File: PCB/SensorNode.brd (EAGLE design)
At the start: 93.6 x 69.8 mm, 68 parts, among them J4 USB_MINI-B_SMT, Q1 CMA-4544PF-W, Q2 600mA/40V, Q3 600mA/40V, U1 MAX4466EXK+T, U2 ESP-WROOM-32, U3 Si7021-A20, U4 MCP73831, U5 TSL2561, U6 CP2104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

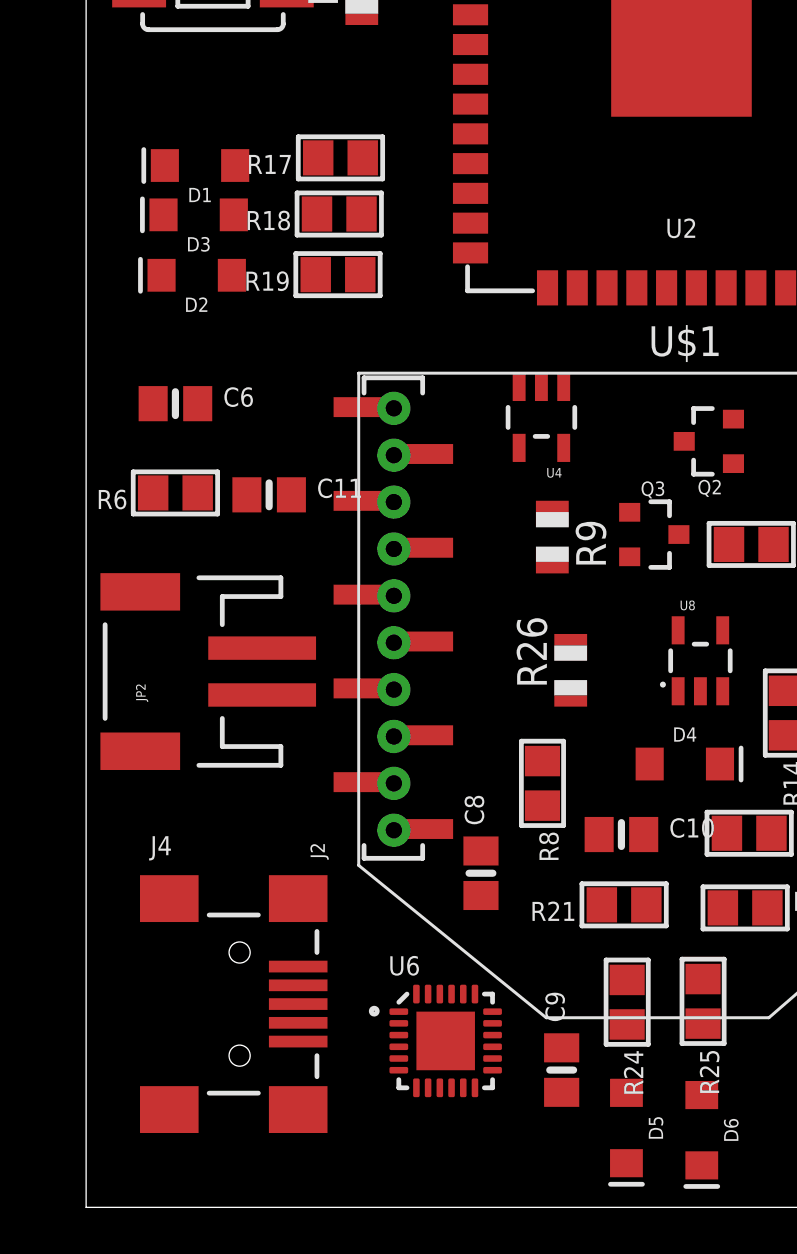
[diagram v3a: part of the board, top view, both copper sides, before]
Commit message: Created Android Wear App
Sets the smart watch's bluetooth to discoverable.
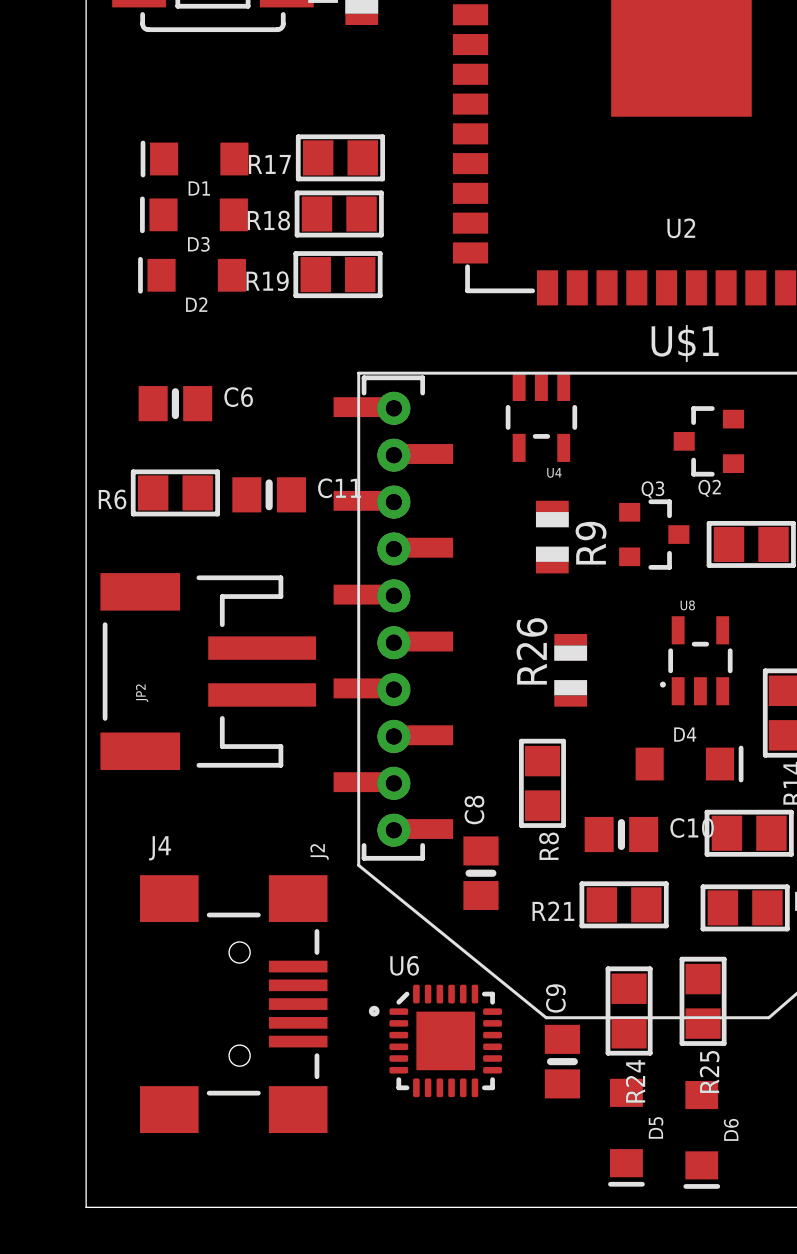
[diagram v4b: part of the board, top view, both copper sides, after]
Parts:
- moved R24 0.39 mm to (21.9, 41.4)
- moved C9 0.36 mm to (19.1, 39.2)
- moved D1 0.28 mm to (3.56, 77.7)
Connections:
- net VIN renamed VBUS
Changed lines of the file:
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@@
 <attribute name="PROD_ID" value="BATT-13243" x="-8.066809375" y="98.5227625" size="1.778" layer="27" rot="R180" display="off"/>
 </element>
-<element name="D1" library="SparkFun-LED" package="LED-1206" value="BLUE" x="3.590128125" y="77.468071875" rot="R180">
-<attribute name="PROD_ID" value="DIO-09911" x="3.590128125" y="77.468071875" size="1.778" layer="27" rot="R180" display="off"/>
+<element name="D1" library="SparkFun-LED" package="LED-1206" value="BLUE" x="3.557346875" y="77.746625" rot="R180">
+<attribute name="PROD_ID" value="DIO-09911" x="3.557346875" y="77.746625" size="1.778" layer="27" rot="R180" display="off"/>
 </element>
 <element name="D2" library="SparkFun-LED" package="LED-1206" value="GREEN" x="3.448509375" y="72.785596875" rot="R180">
@@
 <attribute name="PROD_ID" value="DIO-00862" x="24.996034375" y="36.311871875" size="1.778" layer="27" rot="R270" display="off"/>
 </element>
-<element name="R24" library="microbuilder" package="0805" value="???" x="21.813565625" y="41.774221875" rot="R270"/>
+<element name="R24" library="microbuilder" package="0805" value="???" x="21.89551875" y="41.397359375" rot="R270"/>
 <element name="R25" library="microbuilder" package="0805" value="???" x="25.051178125" y="41.810359375" rot="R270"/>
-<element name="C9" library="microbuilder" package="0805-NO" value="4.7uF" x="19.0186" y="38.877525" rot="R90"/>
+<element name="C9" library="microbuilder" package="0805-NO" value="4.7uF" x="19.05138125" y="39.238003125" rot="R90"/>
 <element name="R8" library="microbuilder" package="0805" value="4.7K" x="18.199771875" y="51.10983125" rot="R270"/>
 <element name="C11" library="microbuilder" package="0805-NO" value="0.1uF" x="6.538284375" y="63.41988125"/>
@@
 <wire x1="12.070421875" y1="40.870465625" x2="15.575896875" y2="46.32528125" width="0" layer="19" extent="1-1"/>
 <wire x1="7.778903125" y1="40.093175" x2="12.070421875" y2="40.870465625" width="0" layer="19" extent="1-1"/>
-<wire x1="19.0186" y1="37.927525" x2="12.070421875" y2="40.870465625" width="0" layer="19" extent="1-1"/>
-<wire x1="21.78253125" y1="34.9056" x2="19.0186" y2="37.927525" width="0" layer="19" extent="1-1"/>
+<wire x1="19.05138125" y1="38.288003125" x2="12.070421875" y2="40.870465625" width="0" layer="19" extent="1-1"/>
+<wire x1="21.78253125" y1="34.9056" x2="19.05138125" y2="38.288003125" width="0" layer="19" extent="1-1"/>
 <wire x1="24.996034375" y1="34.811871875" x2="21.78253125" y2="34.9056" width="0" layer="19" extent="1-1"/>
 <wire x1="32.40484375" y1="34.432371875" x2="24.996034375" y2="34.811871875" width="0" layer="19" extent="1-1"/>
@@
 <wire x1="1.948509375" y1="72.785596875" x2="1.59" y2="67.31" width="0" layer="19" extent="1-1"/>
 <wire x1="2.03210625" y1="75.364025" x2="1.948509375" y2="72.785596875" width="0" layer="19" extent="1-1"/>
-<wire x1="2.090128125" y1="77.468071875" x2="2.03210625" y2="75.364025" width="0" layer="19" extent="1-1"/>
+<wire x1="2.057346875" y1="77.746625" x2="2.03210625" y2="75.364025" width="0" layer="19" extent="1-1"/>
 <wire x1="6.24" y1="54.88" x2="7.488284375" y2="63.41988125" width="0" layer="19" extent="1-1"/>
 <wire x1="15.13" y1="90.25" x2="26.67" y2="100.33" width="0" layer="19" extent="1-1"/>
@@
 <contactref element="U2" pad="27"/>
 </signal>
-<signal name="VIN">
+<signal name="VBUS">
 <contactref element="U4" pad="4"/>
 <contactref element="R21" pad="1"/>
@@
 <contactref element="R17" pad="2"/>
 <contactref element="D1" pad="A"/>
-<wire x1="5.090128125" y1="77.468071875" x2="8.631190625" y2="77.7948125" width="0" layer="19" extent="1-1"/>
+<wire x1="5.057346875" y1="77.746625" x2="8.631190625" y2="77.7948125" width="0" layer="19" extent="1-1"/>
 </signal>
 <signal name="N$27">
@@
 <contactref element="D5" pad="A"/>
 <contactref element="R24" pad="2"/>
-<wire x1="21.78253125" y1="37.9056" x2="21.813565625" y2="40.824221875" width="0" layer="19" extent="1-1"/>
+<wire x1="21.78253125" y1="37.9056" x2="21.89551875" y2="40.447359375" width="0" layer="19" extent="1-1"/>
 </signal>
 <signal name="N$42">
 <contactref element="U6" pad="14"/>
 <contactref element="R24" pad="1"/>
-<wire x1="16.070421875" y1="39.370465625" x2="21.813565625" y2="42.724221875" width="0" layer="19" extent="1-1"/>
+<wire x1="16.070421875" y1="39.370465625" x2="21.89551875" y2="42.347359375" width="0" layer="19" extent="1-1"/>
 </signal>
 <signal name="N$43">
@@
 <contactref element="U6" pad="16"/>
 <contactref element="C9" pad="2"/>
-<wire x1="16.070421875" y1="40.370465625" x2="19.0186" y2="39.827525" width="0" layer="19" extent="1-1"/>
+<wire x1="16.070421875" y1="40.370465625" x2="19.05138125" y2="40.188003125" width="0" layer="19" extent="1-1"/>
 </signal>
 <signal name="N$11">

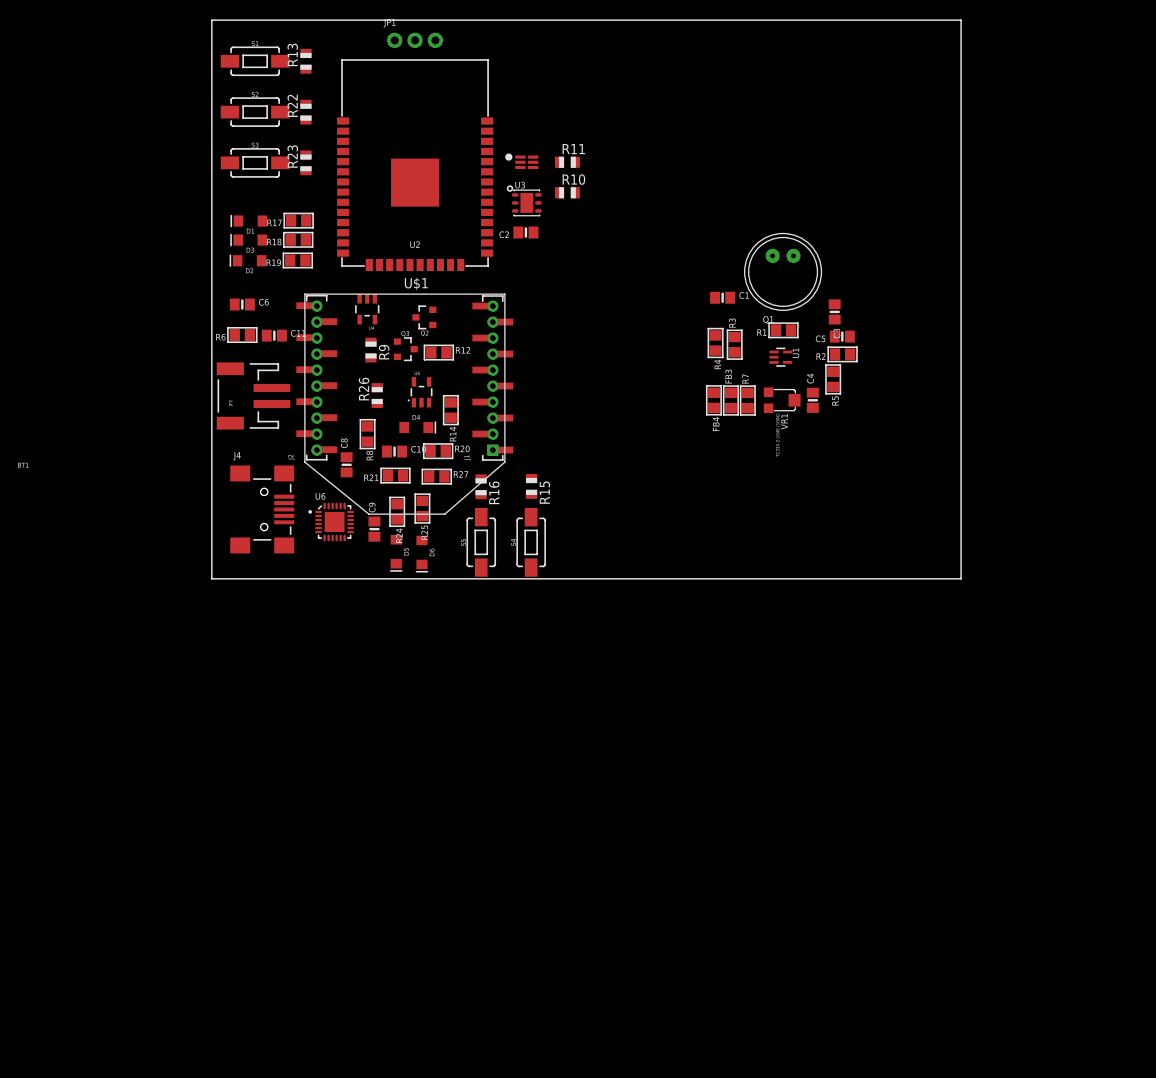
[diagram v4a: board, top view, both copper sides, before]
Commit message: Fixed Net Issues, Started Routing
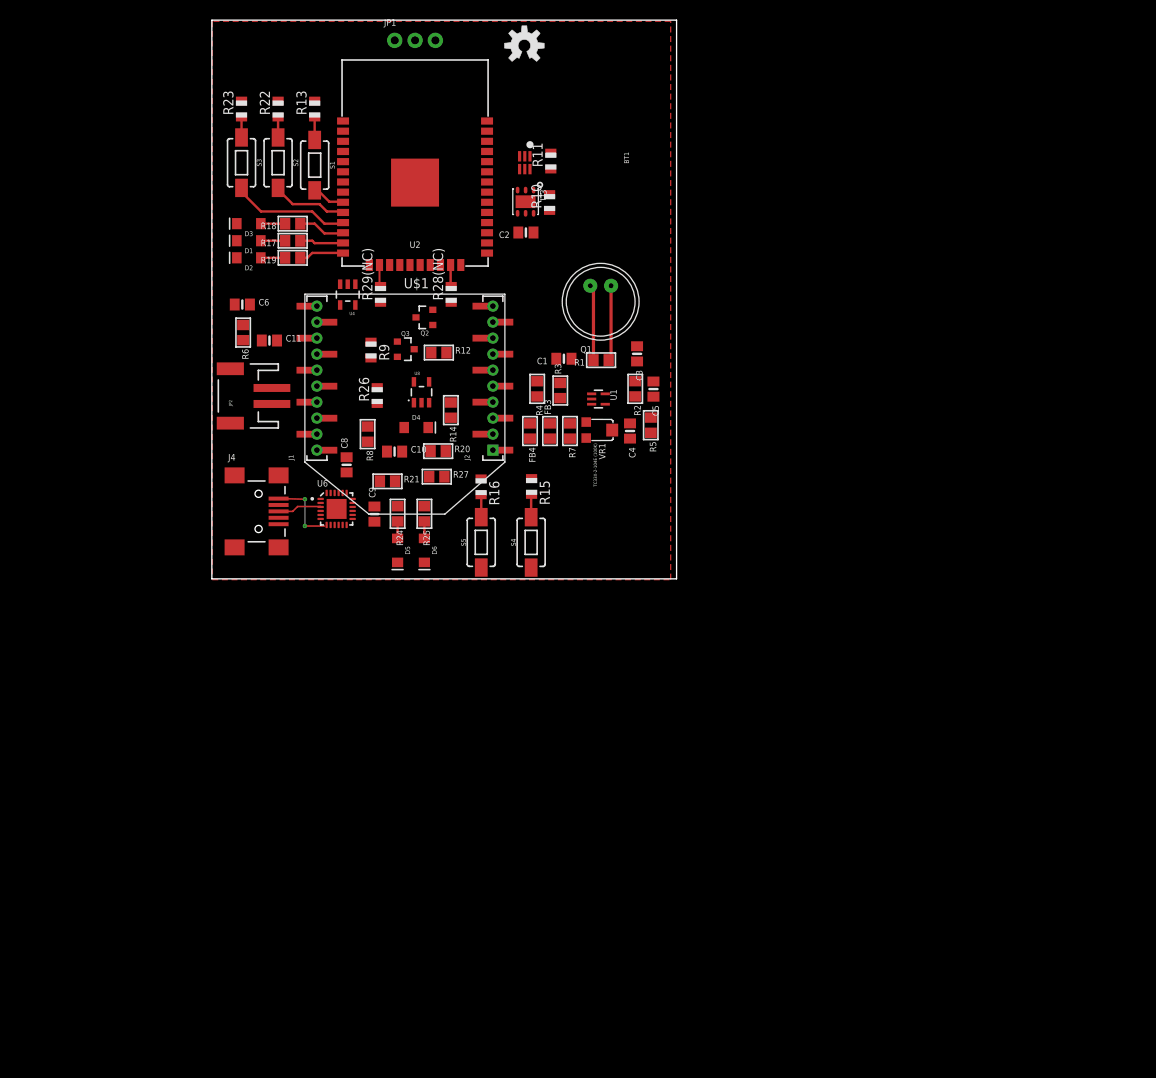
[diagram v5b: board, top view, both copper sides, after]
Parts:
- added FRAME1: FRAME-LEDGER, SparkFun-Aesthetics:CREATIVE_COMMONS
- added LOGO1: OSHW-LOGOM, SparkFun-Aesthetics:OSHW-LOGO-M
- added R28(NC), R29(NC): 0k, adafruit:R0805
- moved R2 26.3 mm to (51.7, 56.8), turned to 270 degrees
- moved C3 25.3 mm to (51.9, 61.1)
- moved C5 24.5 mm to (53.9, 56.7), turned to 270 degrees
- moved R5 23.5 mm to (53.6, 52.2)
- moved U1 23.4 mm to (47.1, 55.5)
- moved FB4 23.3 mm to (38.5, 51.5)
- moved C4 23.2 mm to (51.0, 51.5), turned to 270 degrees
- moved R1 23.1 mm to (47.4, 60.4)
- moved Q1 23.1 mm to (47.3, 67.7)
- moved VR1 23.1 mm to (47.3, 51.6)
- moved R4 23.0 mm to (39.4, 56.8)
- moved FB3 22.9 mm to (41.0, 51.5)
- moved R7 22.6 mm to (43.5, 51.5), turned to 270 degrees
- moved R3 22.5 mm to (42.3, 56.6)
- moved J2 22.0 mm to (33.9, 49.1)
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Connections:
- removed net N$1: U2.17
- removed net N$12: U2.18
- removed net N$15: C6.2, R6.1
- removed net N$17: U2.21
- removed net N$18: U2.22
- removed net N$19: U2.28
- removed net N$2: U3.6
- removed net N$20: U2.6
- removed net N$21: U2.7
- removed net N$22: U2.27
- removed net N$24: R15.2, S4.2
- removed net N$28: R18.1
- removed net N$29: R17.1
- removed net N$30: R19.1
- removed net N$31: S1.2
- removed net N$32: S2.2
- removed net N$33: S3.2
- removed net N$34: R20.2, R27.1
- removed net N$38: R16.2, S5.2
- removed net N$39: U6.21
- removed net N$4: U3.1
- removed net N$40: U6.20
- removed net N$46: Q3.3
- removed net N$47: Q2.3
- removed net N$48: R9.1
- removed net N$49: R26.1
- removed net N$6: U2.19
- new net CTS: R28(NC).1, U6.18
- new net IO13: R29(NC).2, U2.16
- new net IO15: R28(NC).2, U2.23
- net DTR: now also R9.1
- net EN: now also C6.2, Q3.3, R16.2, R6.1, S5.2
- net IO0: now also Q2.3, R15.2, S4.2
- net IO12: now also R19.1
- net IO14: now also R17.1
- net IO25: now also S2.2
- net IO26: now also S3.2
- net IO27: now also R18.1
- net IO32: now also R20.2, R27.1
- net IO33: now also S1.2
- net IO34: now also U2.6
- net IO35: now also U2.7
- net IO8: now also U2.21, U2.22
- net RTS: now also R26.1, R29(NC).1, U6.20
- net RTS1: now also U2.19
- net RXD0: now also U6.21
- net RXD1: now also U2.17
- net SCL: now also U2.28, U3.6
- net SDA: now also U2.27, U3.1
- net TXD1: now also U2.18
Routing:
- net IO26: track 0.00 -> 14.9 mm
- net AGND: track 0.00 -> 10.00 mm
- net N$3: track 0.00 -> 9.60 mm
- net IO25: track 0.00 -> 9.52 mm
- net VBUS: track 0.00 -> 9.08 mm, vias 0 -> 2
- net N$35: track 0.00 -> 7.97 mm
- net IO27: track 0.00 -> 5.88 mm
- net IO12: track 0.00 -> 5.60 mm
- net N$37: track 0.00 -> 5.53 mm
- net IO14: track 0.00 -> 5.48 mm
- net IO33: track 0.00 -> 4.31 mm
- net N$4: track 0.00 -> 3.05 mm
- net N$2: track 0.00 -> 3.05 mm
- net N$1: track 0.00 -> 3.05 mm
- net IO0: track 0.00 -> 2.86 mm
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- added copper zone on layer 1, net N$17
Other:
- board size 93.6 x 69.8 mm -> 58.1 x 69.8 mm

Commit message: Mid Route Check Point
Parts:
- removed R16: 10K, adafruit:R0805
- removed U$1: XBEE, adafruit:XBEE
- moved S5 65.3 mm to (5.60, 97.2), turned to 180 degrees
- moved C11 58.4 mm to (61.9, 79.3), turned to 180 degrees
- moved R26 45.4 mm to (62.7, 69.5), turned to 0 degrees
- moved R9 44.2 mm to (62.8, 61.2), turned to 0 degrees
- moved Q2 40.9 mm to (66.2, 65.0), turned to 270 degrees
- moved Q3 37.5 mm to (60.2, 65.1), turned to 90 degrees
- moved S4 36.4 mm to (71.6, 53.1), turned to 180 degrees
- moved U5 32.3 mm to (70.2, 84.8), turned to 0 degrees
- moved R10 27.8 mm to (67.4, 88.8), turned to 0 degrees
- moved U3 27.6 mm to (65.2, 84.8)
- moved R11 26.5 mm to (67.3, 81.2), turned to 0 degrees
- moved R15 25.7 mm to (62.3, 54.5), turned to 0 degrees
- moved C2 25.5 mm to (63.1, 81.1)
- moved Q1 20.1 mm to (45.7, 47.6)
- moved C8 19.4 mm to (6.06, 64.1), turned to 270 degrees
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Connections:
- net CTS1: no longer U$1.12
- net EN: no longer R16.2
- net GND: no longer U$1.10
- net IO7: no longer U$1.5
- net IO8: no longer U$1.9
- net RTS1: no longer U$1.16
- net RXD1: no longer U$1.2
- net TXD1: no longer U$1.3
- net VCC: no longer R16.1
- net VCC_3.7V: no longer U$1.1
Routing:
- net VCC_3.7V: track 0.00 -> 78.7 mm
- net TXD1: track 0.00 -> 27.6 mm
- net RXD1: track 0.00 -> 26.5 mm
- net IO35: track 0.00 -> 26.2 mm
- net N$7: track 0.00 -> 19.9 mm
- net AVCC: track 0.41 -> 19.1 mm, vias 0 -> 2
- net AGND: track 10.00 -> 22.5 mm
- net N$5: track 0.00 -> 11.3 mm
- net N$23: track 0.00 -> 9.90 mm
- net VCC: track 0.00 -> 7.17 mm
- net VBUS: track 9.08 -> 15.6 mm
- net IO34: track 0.00 -> 6.45 mm
- net N$43: track 0.00 -> 5.74 mm
- net N$6: track 0.00 -> 5.18 mm
- net N$42: track 0.00 -> 4.48 mm
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
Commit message: Commit Before AutoRouting
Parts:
- removed C11: 0.1uF, microbuilder:0805-NO
- removed R28(NC), R29(NC): 0k, adafruit:R0805
- moved BT1 71.9 mm to (62.7, 68.6)
- moved S5 50.3 mm to (41.2, 61.6)
- moved R10 45.8 mm to (37.4, 54.1), turned to 90 degrees
- moved U3 41.7 mm to (41.2, 50.6), turned to 0 degrees
- moved U5 40.8 mm to (41.4, 55.9), turned to 270 degrees
- moved LOGO1 38.6 mm to (54.0, 64.6)
- moved R26 37.0 mm to (43.5, 37.9), turned to 180 degrees
- moved R21 36.0 mm to (25.4, 12.7), turned to 0 degrees
- moved C2 35.2 mm to (45.6, 50.6), turned to 270 degrees
- moved Q2 34.5 mm to (40.0, 42.5), turned to 90 degrees
- moved R11 34.2 mm to (45.9, 54.4), turned to 90 degrees
- moved R8 34.2 mm to (14.3, 2.73)
- moved JP2 33.7 mm to (3.89, 22.3)
- moved C9 33.4 mm to (26.0, 8.03)
- moved D5 33.4 mm to (30.5, 5.79)
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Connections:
- removed net CTS: R28(NC).1, U6.18
- removed net IO13: R29(NC).2, U2.16
- removed net IO15: R28(NC).2, U2.23
- removed net N$16: U2.20
- removed net N$35: R13.1, R22.1, R23.1, S1.1, S2.1, S3.1
- new net N$24: R13.1, S1.1
- new net N$28: R22.1, S2.1
- new net N$29: R23.1, S3.1
- new net N$32: C3.2, R1.2, R2.1
- net AGND: no longer C3.2, R1.2, R2.1
- net CTS1: now also U2.20
- net GND: no longer C11.2
- net IO7: now also U2.21
- net IO8: no longer U2.21
- net RTS: no longer R29(NC).1, U6.20
- net TXD0: now also U6.20
- net VCC: now also FB4.2, J2.1, JP1.1, R10.2, R11.2, R6.2, U2.2, U5.VDD
- net VCC_3.7V: no longer C11.1, FB4.2, J2.1, JP1.1, R10.2, R11.2, R6.2, U2.2, U5.VDD
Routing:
- net VCC: track 7.17 -> 233.4 mm, vias 0 -> 10
- net EN: track 0.00 -> 87.0 mm, vias 0 -> 2
- net IO0: track 0.00 -> 58.1 mm, vias 0 -> 2
- net RTS: track 0.00 -> 47.3 mm, vias 0 -> 2
- net VCC_3.7V: track 78.7 -> 32.3 mm
- net IO34: track 6.45 -> 42.5 mm, vias 0 -> 2
- net N$16: track 0.00 -> 30.3 mm
- net IO32: track 2.90 -> 28.4 mm
- net IO7: track 0.00 -> 22.1 mm
- net SCL: track 2.16 -> 24.1 mm, vias 0 -> 2
- net VBUS: track 15.6 -> 36.6 mm, vias 2 -> 4
- net RTS1: track 0.00 -> 21.0 mm, vias 0 -> 2
- net SDA: track 2.65 -> 20.9 mm, vias 0 -> 2
- net CTS1: track 0.00 -> 15.5 mm, vias 0 -> 2
- net IO8: track 0.00 -> 14.7 mm
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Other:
- board size 58.1 x 69.8 mm -> 58.9 x 70.1 mm

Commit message: Fully Routed
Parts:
- removed BT1: LIPO-OUTLINE1100, SparkFun-Batteries:LIPO-1000
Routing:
- net GND: track 0.00 -> 322.4 mm, vias 0 -> 8
- net TXD0: track 0.00 -> 50.2 mm, vias 0 -> 2
- net RXD0: track 0.03 -> 47.9 mm, vias 0 -> 2
- net DTR: track 0.02 -> 45.4 mm, vias 0 -> 2
- net N$16: track 30.3 -> 0.00 mm
- net VCC: track 233.4 -> 251.8 mm
- net AGND: track 21.4 -> 36.1 mm, vias 0 -> 1
- net IO34: track 42.5 -> 56.3 mm
- net N$4: track 3.05 -> 0.00 mm
- net N$2: track 3.05 -> 0.00 mm
- net N$1: track 3.05 -> 0.00 mm
- net N$27: track 0.00 -> 3.04 mm
- net N$26: track 0.00 -> 3.04 mm
- net N$25: track 0.00 -> 3.04 mm
- net N$21: track 2.57 -> 0.00 mm
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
